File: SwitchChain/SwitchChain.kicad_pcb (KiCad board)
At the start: 2 copper layers, 20 x 117 mm, 21 parts, among them J101 Conn_01x06, SW1001 SW_Push, SW201 SW_Push, SW301 SW_Push, SW501 SW_Push, SW801 SW_Push, U1101 74HC00, U1102 74HC74, U401 74HC00, U402 74HC74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

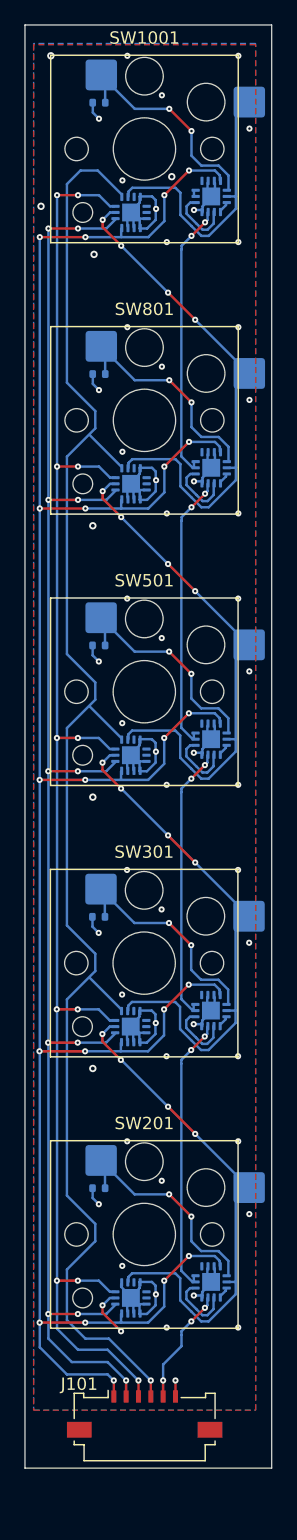
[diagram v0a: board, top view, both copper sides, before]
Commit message: fix pin label, reduce column keys to 4
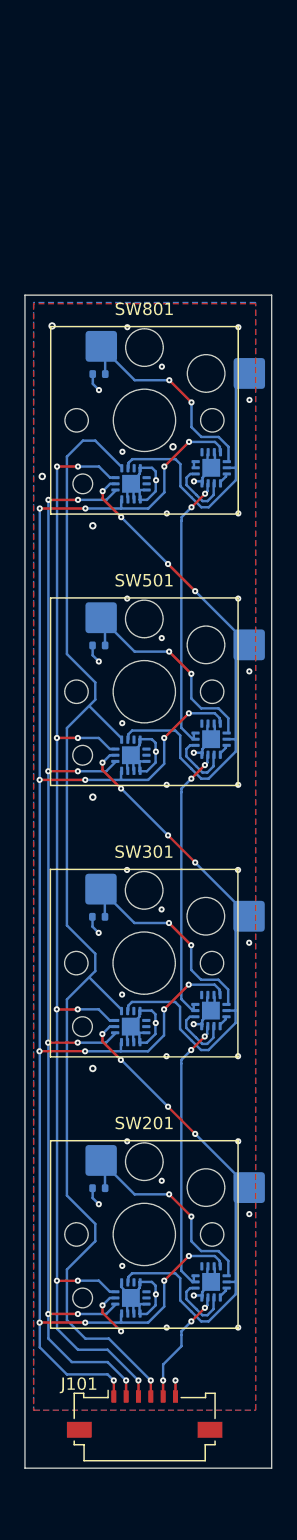
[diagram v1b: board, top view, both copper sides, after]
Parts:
- removed R1001: 40k, Resistor_SMD:R_0402_1005Metric
- removed SW1001: SW_Push, PCM_Switch_Keyboard_Hotswap_Kailh:SW_Hotswap_Kailh_Choc_V1V2_1.00u
- removed U1101: 74HC00, Package_DFN_QFN:WQFN-14-1EP_2.5x2.5mm_P0.5mm_EP1.45x1.45mm
- removed U1102: 74HC74, Package_DFN_QFN:WQFN-14-1EP_2.5x2.5mm_P0.5mm_EP1.45x1.45mm
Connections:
- net Reset renamed ~{Reset}
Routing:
- net ~{Reset}: vias 11 -> 9
- net Vcc: vias 21 -> 17
- net GND: vias 60 -> 49
- net CLK: vias 11 -> 9
- net /SwitchDaisy4/SelectorDaisy/In: vias 2 -> 0
- net /SwitchDaisy3/Select+: vias 4 -> 0
- net /SwitchDaisy3/Out+: vias 2 -> 0
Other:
- board size 20 x 117 mm -> 20 x 95.1 mm

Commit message: fix circuit
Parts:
- added U101: 74HC00, Package_DFN_QFN:WQFN-14-1EP_2.5x2.5mm_P0.5mm_EP1.45x1.45mm, B.Cu at (109.6, 155.6)
- moved J101 3.61 mm to (111.9, 163.2)
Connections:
- U702 pad 1: ~{Reset} -> Vcc
- U702 pad 4: GND -> /SwitchDaisy/~{Init}
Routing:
- net ~{Any}: vias 1 -> 3
- net GND: vias 49 -> 50
- net /SwitchDaisy/~{Init}: vias 0 -> 2
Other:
- board size 20 x 95.1 mm -> 20 x 98.9 mm

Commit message: flip connector
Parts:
- J101: moved to B.Cu
- turned J101 to 180 degrees
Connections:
- J101 pad 1: Vcc -> GND
- J101 pad 2: ~{Reset} -> Out
- J101 pad 3: CLK -> ~{Any}
- J101 pad 4: ~{Any} -> CLK
- J101 pad 5: Out -> ~{Reset}
- J101 pad 6: GND -> Vcc
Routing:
- net ~{Reset}: vias 9 -> 8
- net ~{Any}: vias 3 -> 2
- net Vcc: vias 17 -> 16
- net Out: vias 3 -> 2
- net CLK: vias 9 -> 8
